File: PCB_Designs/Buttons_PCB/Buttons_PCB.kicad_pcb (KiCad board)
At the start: 2 copper layers, 49.5 x 158.8 mm, 68 parts, among them P1 CONN_01X06, U1 CHERRY-MX, U10 CHERRY-MX, U11 CHERRY-MX, U12 CHERRY-MX, U13 MCP23017, U14 MCP23017, U2 CHERRY-MX, U3 CHERRY-MX, U4 CHERRY-MX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

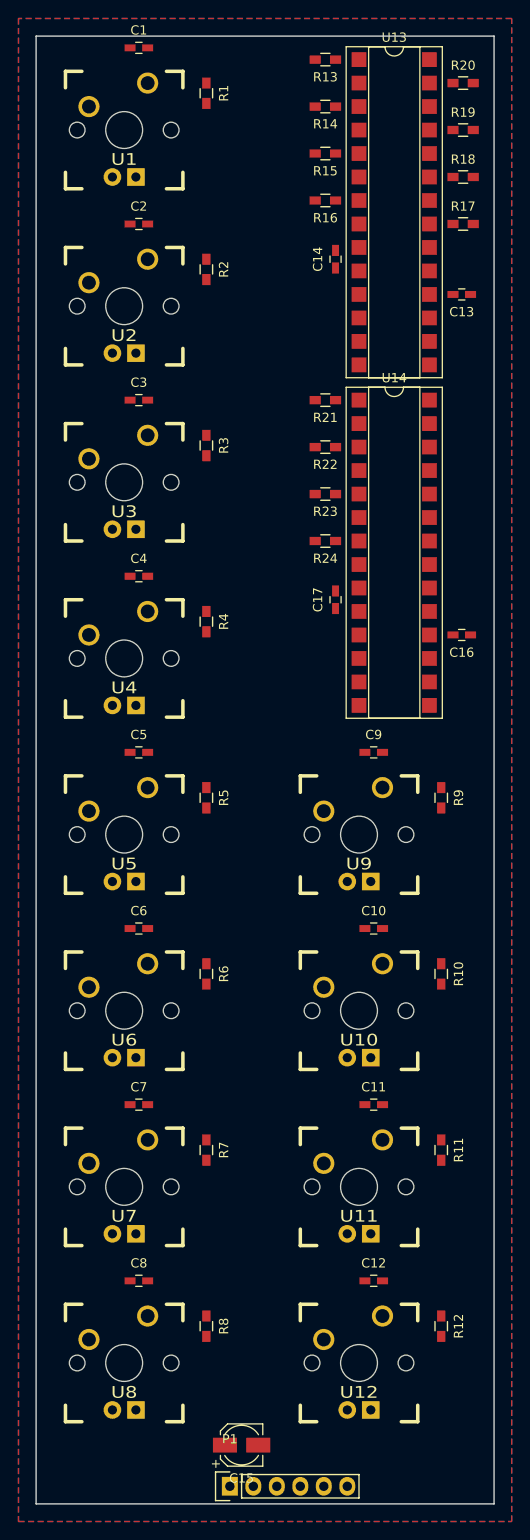
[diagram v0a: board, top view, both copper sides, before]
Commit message: Buttons_PWB_1.0
First edition Buttons_PWB routed (V1.0).
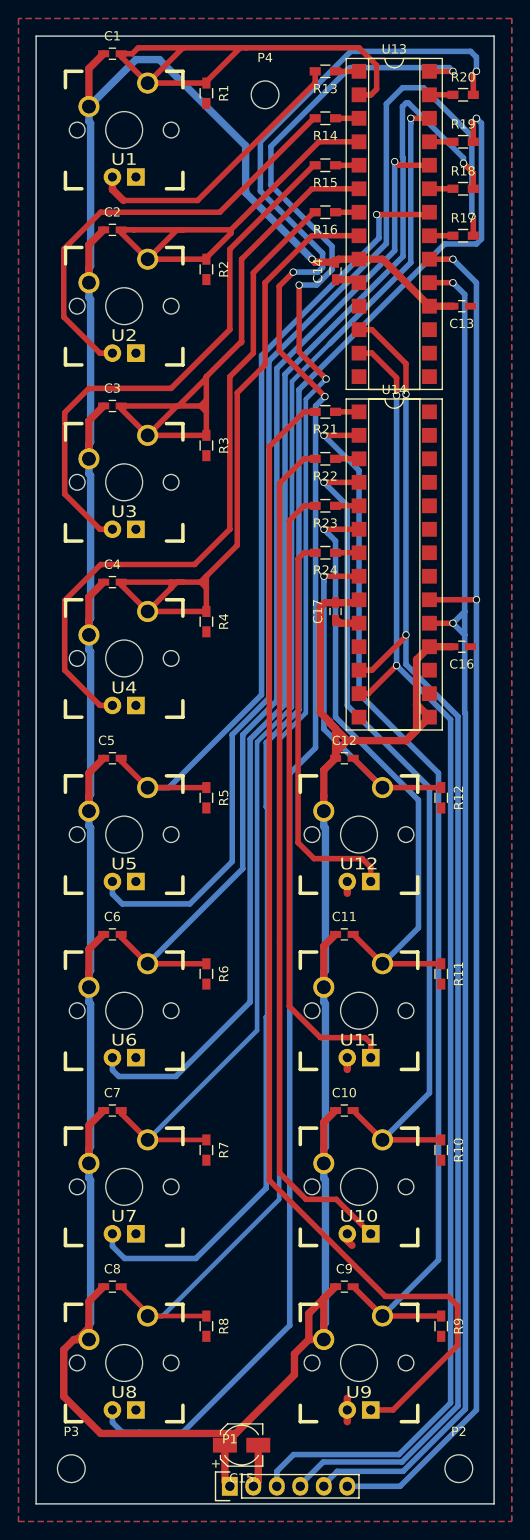
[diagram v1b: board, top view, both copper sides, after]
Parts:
- added P2: CONN_01X01, Mounting_Holes:MountingHole_3mm, F.Cu at (109.9, 180.3)
- added P3: CONN_01X01, Mounting_Holes:MountingHole_3mm, F.Cu at (67.9, 180.3)
- added P4: CONN_01X01, Mounting_Holes:MountingHole_3mm, F.Cu at (88.9, 31.8)
- moved C9 57.9 mm to (97.5, 160.7)
- moved R12 57.2 mm to (108.0, 107.8)
- moved R9 57.2 mm to (108.0, 164.9)
- moved D12 57.1 mm to (99.1, 111.8)
- moved D9 57.1 mm to (99.1, 168.9)
- moved U12 57.1 mm to (99.1, 111.8)
- moved U9 57.1 mm to (99.1, 168.9)
- moved C12 56.6 mm to (97.5, 103.5)
- moved C10 19.9 mm to (97.5, 141.6)
- moved D10 19.1 mm to (99.1, 149.9)
- moved D11 19.1 mm to (99.1, 130.8)
- moved U10 19.1 mm to (99.1, 149.9)
- moved U11 19.1 mm to (99.1, 130.8)
- moved R10 19.0 mm to (108.0, 145.9)
- moved R11 19.0 mm to (108.0, 126.8)
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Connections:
- P1 pad 3: /S_CLK_L -> /S_DAT_L
- P1 pad 4: /S_DAT_L -> /S_CLK_L
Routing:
- net /VDD: track 0.00 -> 433.4 mm, vias 0 -> 1
- net Net-(D8-Pad1): track 0.00 -> 195.6 mm, vias 0 -> 3
- net Net-(C8-Pad2): track 0.00 -> 178.6 mm, vias 0 -> 3
- net Net-(D7-Pad1): track 0.00 -> 152.1 mm, vias 0 -> 1
- net /intA: track 0.00 -> 150.5 mm, vias 0 -> 2
- net /intB: track 0.00 -> 149.9 mm, vias 0 -> 2
- net /S_CLK_L: track 0.00 -> 149.1 mm, vias 0 -> 2
- net /S_DAT_L: track 0.00 -> 147.4 mm, vias 0 -> 2
- net Net-(D6-Pad1): track 0.00 -> 136.6 mm, vias 0 -> 1
- net Net-(C7-Pad2): track 0.00 -> 135.0 mm, vias 0 -> 1
- net Net-(D5-Pad1): track 0.00 -> 128.5 mm, vias 0 -> 1
- net Net-(D9-Pad2): track 0.00 -> 128.4 mm
- net Net-(C9-Pad2): track 0.00 -> 117.5 mm, vias 0 -> 1
- net Net-(C6-Pad2): track 0.00 -> 112.5 mm, vias 0 -> 1
- net Net-(C10-Pad2): track 0.00 -> 92.6 mm, vias 0 -> 1
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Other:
- net class Default: trace_width 0.25 -> 0.5; via_dia 0.6 -> 0.8; via_drill 0.4 -> 0.6
- rule via_min_drill: 0.3 -> 0.6

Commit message: Buttons_PCB v2
Changed order of buttons 5-8 to prevent vias below SMD extenders.
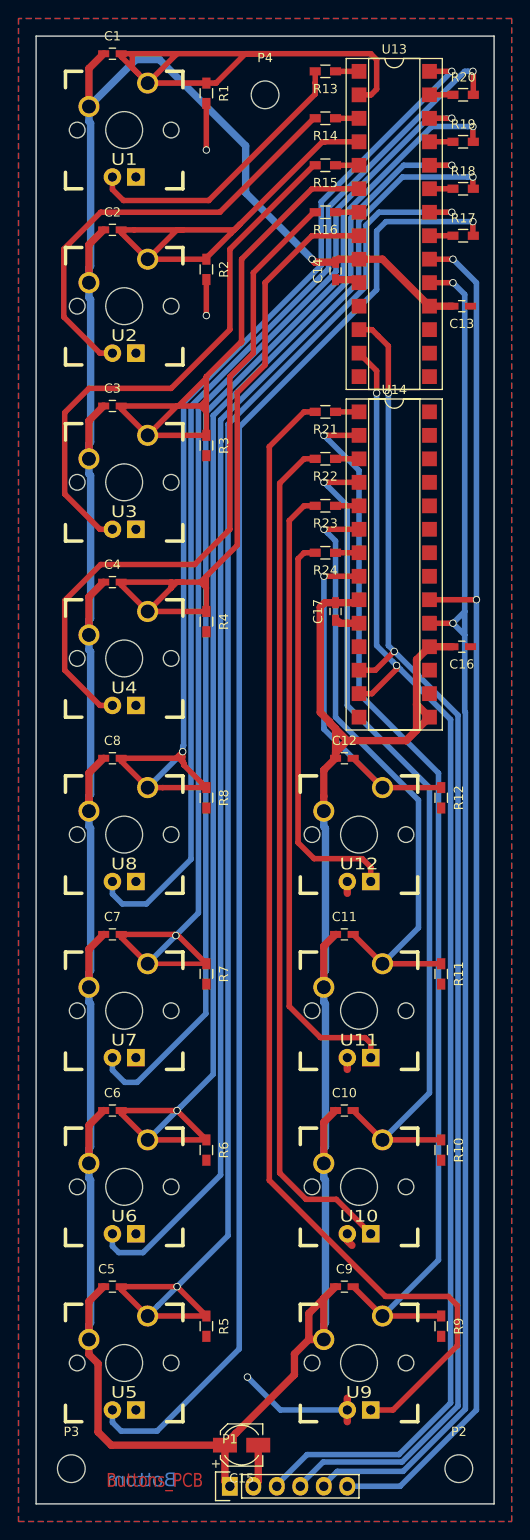
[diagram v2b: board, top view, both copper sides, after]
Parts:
- moved C5 57.2 mm to (72.4, 160.7)
- moved C8 57.2 mm to (72.4, 103.5)
- moved R5 57.2 mm to (82.5, 164.9)
- moved R8 57.2 mm to (82.5, 107.8)
- moved D5 57.1 mm to (73.7, 168.9)
- moved D8 57.1 mm to (73.7, 111.8)
- moved U5 57.1 mm to (73.7, 168.9)
- moved U8 57.1 mm to (73.7, 111.8)
- moved D6 19.1 mm to (73.7, 149.9)
- moved D7 19.1 mm to (73.7, 130.8)
- moved U6 19.1 mm to (73.7, 149.9)
- moved U7 19.1 mm to (73.7, 130.8)
- moved R6 19.0 mm to (82.5, 145.9)
- moved R7 19.0 mm to (82.5, 126.8)
- moved C6 19.0 mm to (72.4, 141.6)
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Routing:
- net Net-(D8-Pad1): track 195.6 -> 113.2 mm, vias 3 -> 1
- net Net-(C5-Pad2): track 90.3 -> 161.6 mm, vias 1 -> 2
- net Net-(C8-Pad2): track 178.6 -> 117.4 mm, vias 3 -> 2
- net Net-(C6-Pad2): track 112.5 -> 145.7 mm, vias 1 -> 2
- net Net-(D5-Pad1): track 128.5 -> 158.7 mm
- net Net-(D7-Pad1): track 152.1 -> 127.3 mm
- net /GND: track 16.4 -> 37.6 mm, vias 0 -> 3
- net /VDD: track 433.4 -> 427.5 mm
- net Net-(D6-Pad1): track 136.6 -> 141.8 mm
- net Net-(C7-Pad2): track 135.0 -> 130.2 mm, vias 1 -> 2
- net Net-(C1-Pad2): track 54.8 -> 59.0 mm
- net /S_CLK_L: track 149.1 -> 147.1 mm
- net /S_DAT_L: track 147.4 -> 145.8 mm
- net Net-(C2-Pad2): track 49.8 -> 50.8 mm
- net Net-(D1-Pad1): track 30.3 -> 31.0 mm
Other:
- board text added: "Bottom"
- board text added: "Buttons_PCB"

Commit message: ...
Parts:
- moved C16 1.87 mm to (108.8, 92.7), turned to 90 degrees
- moved C13 1.59 mm to (109.2, 55.9), turned to 90 degrees
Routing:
- net /GND: track 37.6 -> 42.5 mm
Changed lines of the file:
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@@
     (links 138)
     (no_connects 0)
-    (area 64.059999 25.324999 113.740001 184.225001)
+    (area 48.585716 18.255001 122.779838 186.65)
     (thickness 1.6)
     (drawings 11)
-    (tracks 520)
+    (tracks 526)
     (zones 0)
     (modules 71)
@@
   )
   (setup
-    (last_trace_width 0.6)
+    (last_trace_width 0.8)
     (user_trace_width 0.5)
     (user_trace_width 0.6)
@@
   )
   (module Capacitors_SMD:C_0603_HandSoldering (layer F.Cu)
-    (at 110.17 54.61 180)
+    (at 109.1946 55.8698 90)
     (descr "Capacitor SMD 0603, hand soldering")
     (tags "capacitor 0603")
     (attr smd)
-    (fp_text reference C13 (at 0 -1.9 180) (layer F.SilkS)
-      (effects (font (size 1 1) (thickness 0.15)))
-    )
-    (fp_text value 100n (at 0 1.9 180) (layer F.Fab)
+    (fp_text reference C13 (at 0 -1.9 90) (layer F.SilkS)
+      (effects (font (size 1 1) (thickness 0.15)))
+    )
+    (fp_text value 100n (at 0 1.9 90) (layer F.Fab)
       (effects (font (size 1 1) (thickness 0.15)))
     )
@@
     (fp_line (start -0.35 -0.6) (end 0.35 -0.6) (layer F.SilkS) (width 0.12))
     (fp_line (start 0.35 0.6) (end -0.35 0.6) (layer F.SilkS) (width 0.12))
-    (pad 1 smd rect (at -0.95 0 180) (size 1.2 0.75) (layers F.Cu F.Paste F.Mask)
-      (net 14 /GND))
-    (pad 2 smd rect (at 0.95 0 180) (size 1.2 0.75) (layers F.Cu F.Paste F.Mask)
+    (pad 1 smd rect (at -0.95 0 90) (size 1.2 0.75) (layers F.Cu F.Paste F.Mask)
+      (net 14 /GND))
+    (pad 2 smd rect (at 0.95 0 90) (size 1.2 0.75) (layers F.Cu F.Paste F.Mask)
       (net 1 /VDD))
     (model Capacitors_SMD.3dshapes/C_0603_HandSoldering.wrl
@@
   )
   (module Capacitors_SMD:C_0603_HandSoldering (layer F.Cu)
-    (at 110.17 91.44 180)
+    (at 108.7882 92.6948 90)
     (descr "Capacitor SMD 0603, hand soldering")
     (tags "capacitor 0603")
     (attr smd)
-    (fp_text reference C16 (at 0 -1.9 180) (layer F.SilkS)
-      (effects (font (size 1 1) (thickness 0.15)))
-    )
-    (fp_text value 100n (at 0 1.9 180) (layer F.Fab)
-      (effects (font (size 1 1) (thickness 0.15)))
-    )
-    (fp_line (start -0.8 0.4) (end -0.8 -0.4) (layer F.Fab) (width 0.1))
-    (fp_line (start 0.8 0.4) (end -0.8 0.4) (layer F.Fab) (width 0.1))
-    (fp_line (start 0.8 -0.4) (end 0.8 0.4) (layer F.Fab) (width 0.1))
-    (fp_line (start -0.8 -0.4) (end 0.8 -0.4) (layer F.Fab) (width 0.1))
-    (fp_line (start -1.85 -0.75) (end 1.85 -0.75) (layer F.CrtYd) (width 0.05))
-    (fp_line (start -1.85 0.75) (end 1.85 0.75) (layer F.CrtYd) (width 0.05))
-    (fp_line (start -1.85 -0.75) (end -1.85 0.75) (layer F.CrtYd) (width 0.05))
-    (fp_line (start 1.85 -0.75) (end 1.85 0.75) (layer F.CrtYd) (width 0.05))
-    (fp_line (start -0.35 -0.6) (end 0.35 -0.6) (layer F.SilkS) (width 0.12))
-    (fp_line (start 0.35 0.6) (end -0.35 0.6) (layer F.SilkS) (width 0.12))
-    (pad 1 smd rect (at -0.95 0 180) (size 1.2 0.75) (layers F.Cu F.Paste F.Mask)
-      (net 14 /GND))
-    (pad 2 smd rect (at 0.95 0 180) (size 1.2 0.75) (layers F.Cu F.Paste F.Mask)
-      (net 1 /VDD))
-    (model Capacitors_SMD.3dshapes/C_0603_HandSoldering.wrl
-      (at (xyz 0 0 0))
-      (scale (xyz 1 1 1))
-      (rotate (xyz 0 0 0))
-    )
-  )
-  (module Capacitors_SMD:C_0603_HandSoldering (layer F.Cu)
-    (at 96.52 87.63 90)
-    (descr "Capacitor SMD 0603, hand soldering")
-    (tags "capacitor 0603")
-    (attr smd)
-    (fp_text reference C17 (at 0 -1.9 90) (layer F.SilkS)
+    (fp_text reference C16 (at 0 -1.9 90) (layer F.SilkS)
       (effects (font (size 1 1) (thickness 0.15)))
     )
@@
     )
   )
+  (module Capacitors_SMD:C_0603_HandSoldering (layer F.Cu)
+    (at 96.52 87.63 90)
+    (descr "Capacitor SMD 0603, hand soldering")
+    (tags "capacitor 0603")
+    (attr smd)
+    (fp_text reference C17 (at 0 -1.9 90) (layer F.SilkS)
+      (effects (font (size 1 1) (thickness 0.15)))
+    )
+    (fp_text value 100n (at 0 1.9 90) (layer F.Fab)
+      (effects (font (size 1 1) (thickness 0.15)))
+    )
+    (fp_line (start -0.8 0.4) (end -0.8 -0.4) (layer F.Fab) (width 0.1))
+    (fp_line (start 0.8 0.4) (end -0.8 0.4) (layer F.Fab) (width 0.1))
+    (fp_line (start 0.8 -0.4) (end 0.8 0.4) (layer F.Fab) (width 0.1))
+    (fp_line (start -0.8 -0.4) (end 0.8 -0.4) (layer F.Fab) (width 0.1))
+    (fp_line (start -1.85 -0.75) (end 1.85 -0.75) (layer F.CrtYd) (width 0.05))
+    (fp_line (start -1.85 0.75) (end 1.85 0.75) (layer F.CrtYd) (width 0.05))
+    (fp_line (start -1.85 -0.75) (end -1.85 0.75) (layer F.CrtYd) (width 0.05))
+    (fp_line (start 1.85 -0.75) (end 1.85 0.75) (layer F.CrtYd) (width 0.05))
+    (fp_line (start -0.35 -0.6) (end 0.35 -0.6) (layer F.SilkS) (width 0.12))
+    (fp_line (start 0.35 0.6) (end -0.35 0.6) (layer F.SilkS) (width 0.12))
+    (pad 1 smd rect (at -0.95 0 90) (size 1.2 0.75) (layers F.Cu F.Paste F.Mask)
+      (net 14 /GND))
+    (pad 2 smd rect (at 0.95 0 90) (size 1.2 0.75) (layers F.Cu F.Paste F.Mask)
+      (net 1 /VDD))
+    (model Capacitors_SMD.3dshapes/C_0603_HandSoldering.wrl
+      (at (xyz 0 0 0))
+      (scale (xyz 1 1 1))
+      (rotate (xyz 0 0 0))
+    )
+  )
   (module Mounting_Holes:MountingHole_3mm (layer F.Cu)
     (at 109.855 180.34)
@@
   (gr_line (start 113.665 25.4) (end 64.135 25.4) (layer Edge.Cuts) (width 0.15))
   (segment (start 90.426044 123.450633) (end 90.424 123.448589) (width 0.5) (layer B.Cu) (net 0))
+  (segment (start 106.68 91.44) (end 108.4834 91.44) (width 0.8) (layer F.Cu) (net 1))
+  (segment (start 108.4834 91.44) (end 108.7882 91.7448) (width 0.8) (layer F.Cu) (net 1))
+  (segment (start 109.1946 54.9198) (end 106.9898 54.9198) (width 0.8) (layer F.Cu) (net 1))
+  (segment (start 106.9898 54.9198) (end 106.68 54.61) (width 0.8) (layer F.Cu) (net 1))
   (segment (start 69.85 109.22) (end 69.85 110.882666) (width 0.8) (layer B.Cu) (net 1))
   (segment (start 69.85 110.882666) (end 70.030901 111.063567) (width 0.8) (layer B.Cu) (net 1))
@@
   (segment (start 96.52 86.68) (end 98.74 86.68) (width 0.8) (layer F.Cu) (net 1))
   (segment (start 98.74 86.68) (end 99.06 86.36) (width 0.8) (layer F.Cu) (net 1))
-  (segment (start 106.68 91.44) (end 109.22 91.44) (width 0.8) (layer F.Cu) (net 1))
   (segment (start 96.525 102.875) (end 97.8 101.6) (width 0.8) (layer F.Cu) (net 1))
   (segment (start 97.8 101.6) (end 104.14 101.6) (width 0.8) (layer F.Cu) (net 1))
@@
   (segment (start 95.25 123.83) (end 96.525 122.555) (width 0.8) (layer F.Cu) (net 1))
   (segment (start 95.25 104.78) (end 96.525 103.505) (width 0.8) (layer F.Cu) (net 1))
-  (segment (start 106.68 54.61) (end 109.22 54.61) (width 0.8) (layer F.Cu) (net 1))
   (segment (start 99.06 49.53) (end 101.6 49.53) (width 0.8) (layer F.Cu) (net 1))
   (segment (start 101.6 49.53) (end 106.68 54.61) (width 0.8) (layer F.Cu) (net 1))
@@
   (segment (start 101.6 106.68) (end 107.95 106.68) (width 0.6) (layer F.Cu) (net 13))
   (segment (start 98.425 103.505) (end 101.6 106.68) (width 0.6) (layer F.Cu) (net 13))
+  (segment (start 106.68 93.98) (end 108.453 93.98) (width 0.8) (layer F.Cu) (net 14))
+  (segment (start 108.453 93.98) (end 108.7882 93.6448) (width 0.8) (layer F.Cu) (net 14))
+  (segment (start 106.68 57.15) (end 108.8644 57.15) (width 0.8) (layer F.Cu) (net 14))
+  (segment (start 108.8644 57.15) (end 109.1946 56.8198) (width 0.8) (layer F.Cu) (net 14))
   (segment (start 82.55 32.68) (end 82.55 37.719) (width 0.6) (layer F.Cu) (net 14))
   (via (at 82.55 37.719) (size 0.8) (drill 0.6) (layers F.Cu B.Cu) (net 14))

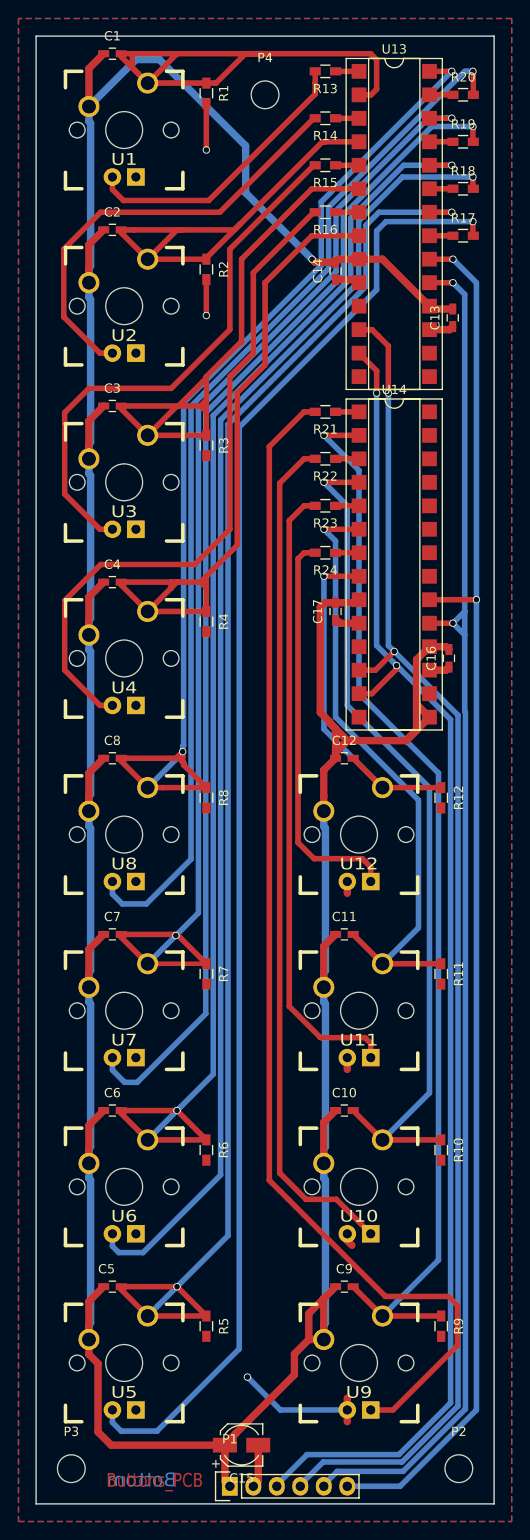
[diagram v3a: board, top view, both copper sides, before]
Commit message: Buttons_V3, Sliders_V2
Easier to manufacture External PCB designs finalized.
Uneccesary footprints library added "Connectors" (Could not find the
regular connector FP, turns out it's the socket-strips)
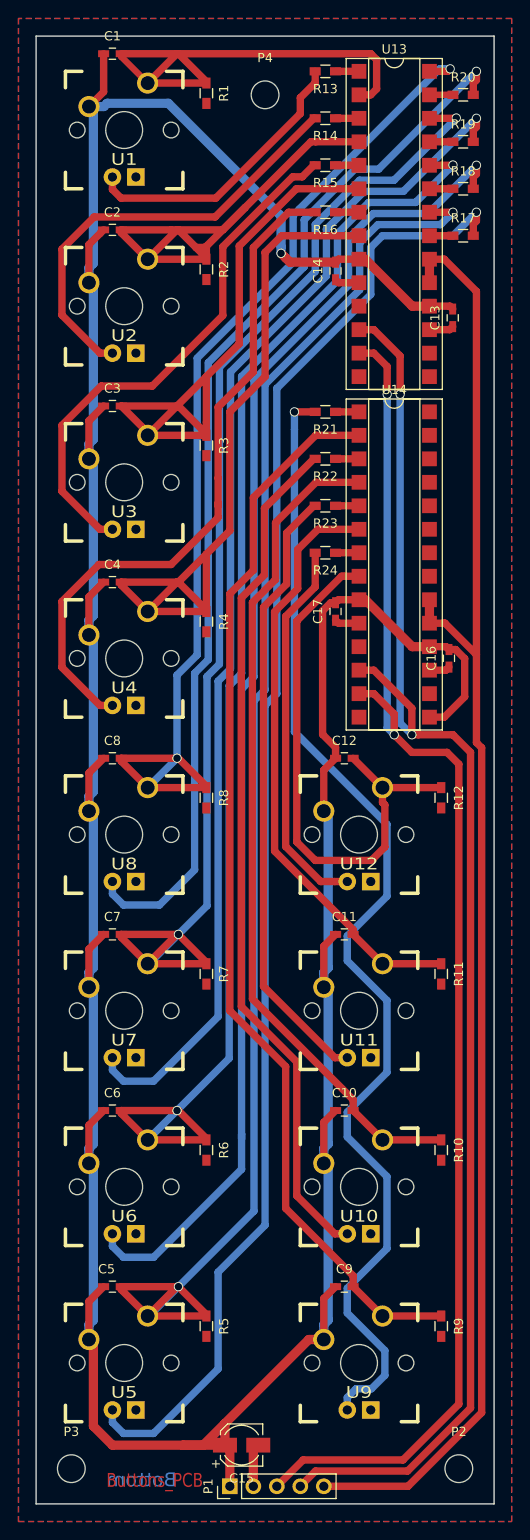
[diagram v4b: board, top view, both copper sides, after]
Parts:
- P1: value CONN_01X06 -> CONN_01X05; footprint Socket_Strips:Socket_Strip_Straight_1x06 -> Socket_Strips:Socket_Strip_Straight_1x05_Pitch2.54mm
- turned P1 to 90 degrees
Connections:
- D10 pad 1: /GND -> Net-(D10-Pad1)
- D10 pad 2: Net-(D10-Pad2) -> /GND
- D11 pad 1: /GND -> Net-(D11-Pad1)
- D11 pad 2: Net-(D11-Pad2) -> /GND
- D12 pad 1: /GND -> Net-(D12-Pad1)
- D12 pad 2: Net-(D12-Pad2) -> /GND
- D9 pad 1: /GND -> Net-(D9-Pad1)
- D9 pad 2: Net-(D9-Pad2) -> /GND
- P1 pad 5: /intB -> /intA
- P2 pad 1: Net-(P2-Pad1) -> (no net)
- P3 pad 1: Net-(P3-Pad1) -> (no net)
- P4 pad 1: Net-(P4-Pad1) -> (no net)
- R21 pad 2: Net-(D9-Pad2) -> Net-(D9-Pad1)
- R22 pad 2: Net-(D10-Pad2) -> Net-(D10-Pad1)
- R23 pad 2: Net-(D11-Pad2) -> Net-(D11-Pad1)
- R24 pad 2: Net-(D12-Pad2) -> Net-(D12-Pad1)
- U13 pad 19: /intB -> /intA
- U14 pad 19: /intB -> /intA
- U14 pad 21: Net-(U14-Pad21) -> (no net)
- U14 pad 22: Net-(U14-Pad22) -> (no net)
- U14 pad 23: Net-(U14-Pad23) -> (no net)
- U14 pad 24: Net-(U14-Pad24) -> (no net)
- U14 pad 25: Net-(U14-Pad25) -> (no net)
- U14 pad 26: Net-(U14-Pad26) -> (no net)
- U14 pad 27: Net-(U14-Pad27) -> (no net)
- U14 pad 28: Net-(U14-Pad28) -> (no net)
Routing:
- net /intB: track 149.9 -> 0.00 mm, vias 2 -> 0
- net Net-(D9-Pad2): track 128.4 -> 0.00 mm
- net Net-(D9-Pad1): track 0.00 -> 127.6 mm, vias 0 -> 1
- net Net-(D10-Pad1): track 0.00 -> 92.8 mm
- net Net-(D10-Pad2): track 92.1 -> 0.00 mm
- net Net-(D11-Pad2): track 68.0 -> 0.00 mm
- net Net-(D11-Pad1): track 0.00 -> 66.6 mm
- net Net-(D12-Pad2): track 43.3 -> 0.00 mm
- net Net-(D12-Pad1): track 0.00 -> 41.3 mm
- net /GND: track 42.5 -> 14.9 mm, vias 3 -> 0
- net Net-(C12-Pad2): track 40.1 -> 61.0 mm, vias 1 -> 0
- net /S_CLK_L: track 147.1 -> 157.4 mm
- net /VDD: track 427.3 -> 417.3 mm
- net /intA: track 150.5 -> 160.0 mm, vias 2 -> 0
- net Net-(C2-Pad2): track 50.8 -> 58.1 mm
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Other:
- net class Default: clearance 0.2 -> 0.4; trace_width 0.5 -> 0.6; via_dia 0.8 -> 1; via_drill 0.6 -> 0.8
- rule trace_clearance: 0.2 -> 0.4
- rule trace_min: 0.5 -> 0.6
- rule via_min_drill: 0.6 -> 0.8
- rule via_min_size: 0.8 -> 1
